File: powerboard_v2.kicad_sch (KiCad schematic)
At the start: 13 parts, among them J4 Conn_01x02_Pin, J5 Conn_01x02_Pin, J6 Conn_01x02_Pin, K1 G6QE-1A DC24, Q1 Q_PMOS, U5 TLP785

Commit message: フットプリントの割り当て
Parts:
- removed Q1: Q_PMOS, symbol Device:Q_PMOS
- added Q2: Q_PMOS_GDS, Package_TO_SOT_THT:TO-220-3_Vertical, symbol Transistor_FET:Q_PMOS_GDS
- C13: footprint (none) -> Capacitor_THT:CP_Radial_D10.0mm_P5.00mm
- D3: footprint (none) -> Diode_SMD:D_SMA
- D4: footprint (none) -> Diode_THT:D_DO-35_SOD27_P7.62mm_Horizontal
- F1: footprint (none) -> Fuse:Fuseholder_Blade_ATO_Littelfuse_Pudenz_2_Pin
- J4: footprint (none) -> Connector_JST:JST_XH_S2B-XH-A-1_1x02_P2.50mm_Horizontal
- J5, J6: footprint (none) -> Connector_AMASS:AMASS_XT60PW-M_1x02_P7.20mm_Horizontal
- R2, R3, R4: footprint (none) -> Resistor_THT:R_Axial_DIN0207_L6.3mm_D2.5mm_P7.62mm_Horizontal
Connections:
- net +24V: now also Q2.2 (D)
- net GND: now also Q2.1 (G)
- net at R4.1: now also Q2.3 (S)
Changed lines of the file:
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@@
+	)
+	(junction
+		(at 78.74 123.19)
+		(diameter 0)
+		(color 0 0 0 0)
 	)
 	(junction
@@
 	(wire
 		(pts
+			(xy 81.28 123.19) (xy 78.74 123.19)
+		)
+		(stroke
+			(width 0)
+			(type default)
+		)
+	)
+	(wire
+		(pts
 			(xy 86.36 35.56) (xy 92.71 35.56)
 		)
@@
 	(wire
 		(pts
+			(xy 78.74 123.19) (xy 78.74 125.73)
+		)
+		(stroke
+			(width 0)
+			(type default)
+		)
+	)
+	(wire
+		(pts
 			(xy 86.36 48.26) (xy 90.17 48.26)
 		)
@@
 	(wire
 		(pts
-			(xy 78.74 120.65) (xy 78.74 125.73)
+			(xy 78.74 120.65) (xy 78.74 123.19)
 		)
 		(stroke
@@
 	(global_label "Photo to Gate"
 		(shape input)
-		(at 78.74 123.19 0)
+		(at 81.28 123.19 0)
 		(fields_autoplaced yes)
 		(effects
@@
 		)
 		(property "Intersheetrefs" "${INTERSHEET_REFS}"
-			(at 95.2111 123.19 0)
+			(at 97.7511 123.19 0)
 			(effects
 				(font
@@
 			)
 		)
-		(property "Footprint" ""
+		(property "Footprint" "Resistor_THT:R_Axial_DIN0207_L6.3mm_D2.5mm_P7.62mm_Horizontal"
 			(at 50.8 113.538 90)
 			(effects
@@
 			)
 		)
-		(property "Footprint" ""
+		(property "Footprint" "Diode_SMD:D_SMA"
 			(at 78.74 90.17 0)
 			(effects
@@
 	)
 	(symbol
+		(lib_id "Transistor_FET:Q_PMOS_GDS")
+		(at 87.63 59.69 0)
+		(unit 1)
+		(exclude_from_sim no)
+		(in_bom yes)
+		(on_board yes)
+		(dnp no)
+		(fields_autoplaced yes)
+		(property "Reference" "Q2"
+			(at 93.98 58.4199 0)
+			(effects
+				(font
+					(size 1.27 1.27)
+				)
+				(justify left)
+			)
+		)
+		(property "Value" "Q_PMOS_GDS"
+			(at 93.98 60.9599 0)
+			(effects
+				(font
+					(size 1.27 1.27)
+				)
+				(justify left)
+			)
+		)
+		(property "Footprint" "Package_TO_SOT_THT:TO-220-3_Vertical"
+			(at 92.71 57.15 0)
+			(effects
+				(font
+					(size 1.27 1.27)
+				)
+				(hide yes)
+			)
+		)
+		(property "Datasheet" "~"
+			(at 87.63 59.69 0)
+			(effects
+				(font
+					(size 1.27 1.27)
+				)
+				(hide yes)
+			)
+		)
+		(property "Description" "P-MOSFET transistor, gate/drain/source"
+			(at 87.63 59.69 0)
+			(effects
+				(font
+					(size 1.27 1.27)
+				)
+				(hide yes)
+			)
+		)
+		(pin "3"
+		)
+		(pin "2"
+		)
+		(pin "1"
+		)
+		(instances
+			(project ""
+				(path "/6e0ca105-c789-4be3-8f3a-c5e169be0bfe"
+					(reference "Q2")
+					(unit 1)
+				)
+			)
+		)
+	)
+	(symbol
 		(lib_id "power:GND")
 		(at 124.46 107.95 0)
@@
 			)
 		)
-		(property "Footprint" ""
+		(property "Footprint" "Capacitor_THT:CP_Radial_D10.0mm_P5.00mm"
 			(at 97.79 47.2948 0)
 			(effects
@@
 			)
 		)
-		(property "Footprint" ""
+		(property "Footprint" "Fuse:Fuseholder_Blade_ATO_Littelfuse_Pudenz_2_Pin"
 			(at 84.582 41.91 90)
 			(effects
@@
 			)
 		)
-		(property "Footprint" ""
+		(property "Footprint" "Connector_JST:JST_XH_S2B-XH-A-1_1x02_P2.50mm_Horizontal"
 			(at 36.83 111.76 0)
 			(effects
@@
 			)
 		)
-		(property "Footprint" ""
+		(property "Footprint" "Resistor_THT:R_Axial_DIN0207_L6.3mm_D2.5mm_P7.62mm_Horizontal"
 			(at 80.518 114.3 90)
 			(effects
@@
 			)
 		)
-		(property "Footprint" ""
+		(property "Footprint" "Diode_THT:D_DO-35_SOD27_P7.62mm_Horizontal"
 			(at 78.74 99.06 0)
 			(effects
@@
 			)
 		)
-		(property "Footprint" ""
+		(property "Footprint" "Resistor_THT:R_Axial_DIN0207_L6.3mm_D2.5mm_P7.62mm_Horizontal"
 			(at 95.25 66.548 90)
 			(effects
@@
 			)
 		)
-		(property "Footprint" ""
+		(property "Footprint" "Connector_AMASS:AMASS_XT60PW-M_1x02_P7.20mm_Horizontal"
 			(at 132.08 97.79 0)
 			(effects
@@
 			)
 		)
-		(property "Footprint" ""
+		(property "Footprint" "Connector_AMASS:AMASS_XT60PW-M_1x02_P7.20mm_Horizontal"
 			(at 95.25 30.48 0)
 			(effects
@@
 					(unit 1)
 				)
-			)
-		)
-	)
-	(symbol
-		(lib_id "Device:Q_PMOS")
-		(at 87.63 59.69 0)
-		(mirror x)
-		(unit 1)
-		(exclude_from_sim no)
-		(in_bom yes)
-		(on_board yes)
-		(dnp no)
-		(property "Reference" "Q1"
-			(at 91.948 56.134 0)
-			(effects
-				(font
-					(size 1.27 1.27)
-				)
-			)
-		)
-		(property "Value" "Q_PMOS"
-			(at 84.328 56.388 0)
-			(effects
-				(font
-					(size 1.27 1.27)
-				)
-			)
-		)
-		(property "Footprint" ""
-			(at 92.71 62.23 0)
-			(effects
-				(font
-					(size 1.27 1.27)
-				)
-				(hide yes)
-			)
-		)
-		(property "Datasheet" "~"
-			(at 87.63 59.69 0)
-			(effects
-				(font
-					(size 1.27 1.27)
-				)
-				(hide yes)
-			)
-		)
-		(property "Description" "P-MOSFET transistor"
-			(at 87.63 59.69 0)
-			(effects
-				(font
-					(size 1.27 1.27)
-				)
-				(hide yes)
-			)
-		)
-		(pin "S"
-		)
-		(pin "D"
-		)
-		(pin "G"
-		)
-		(instances
-			(project ""
-				(path "/6e0ca105-c789-4be3-8f3a-c5e169be0bfe"
-					(reference "Q1")
-					(unit 1)
-				)

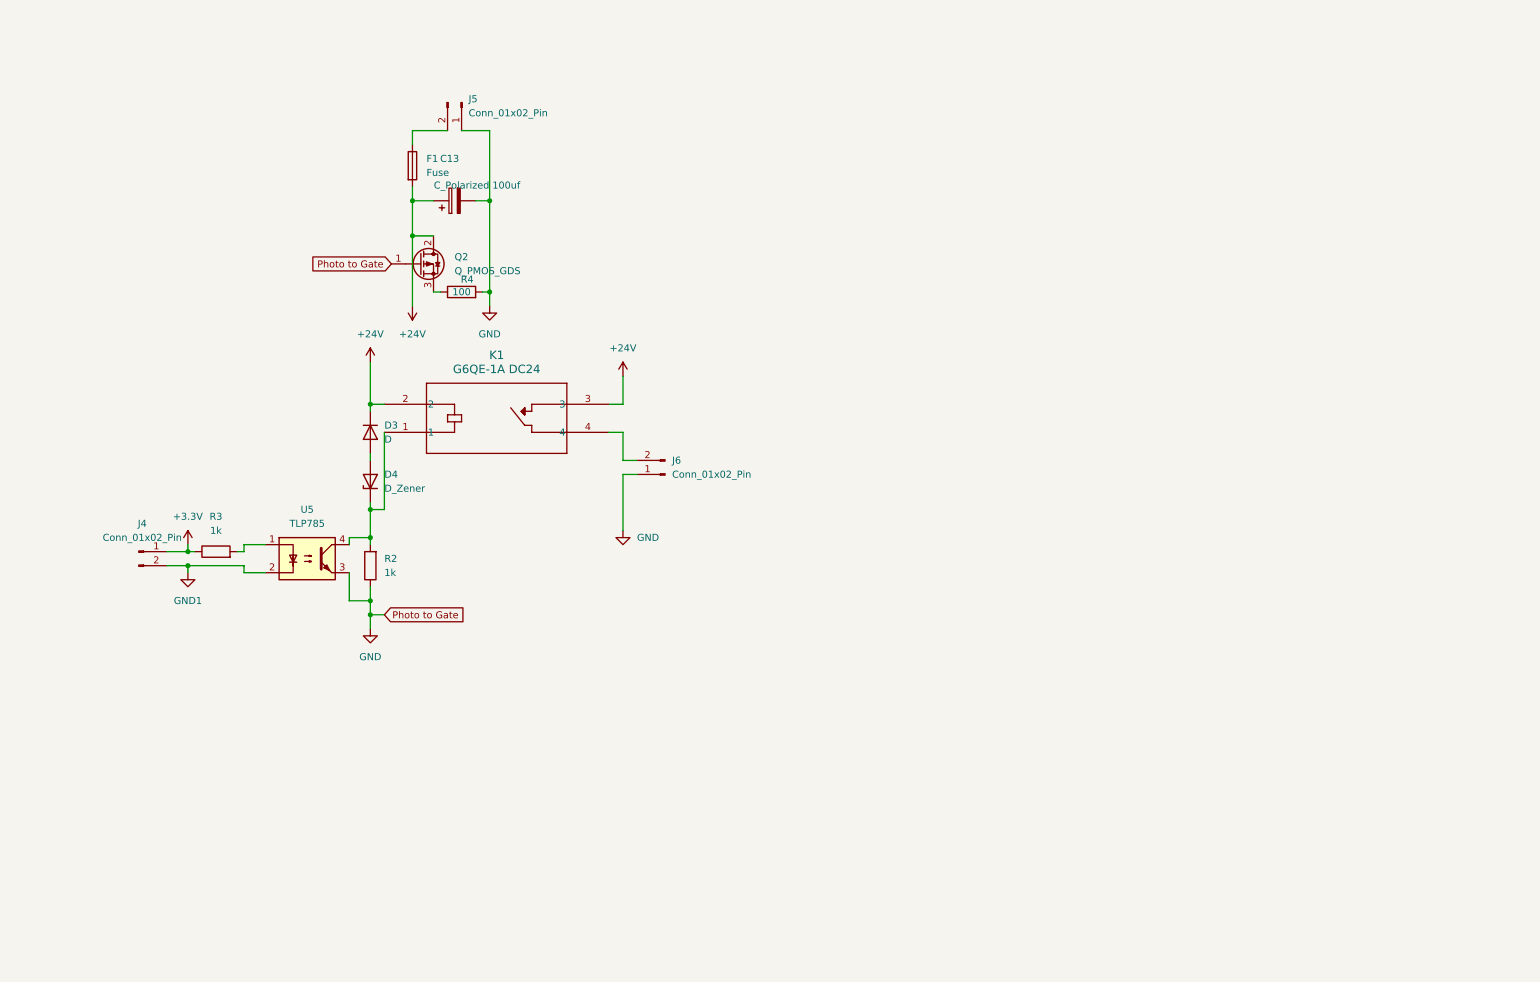
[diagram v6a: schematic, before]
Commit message: 回路構成の変更、フットプリントの割り当て、部品配置
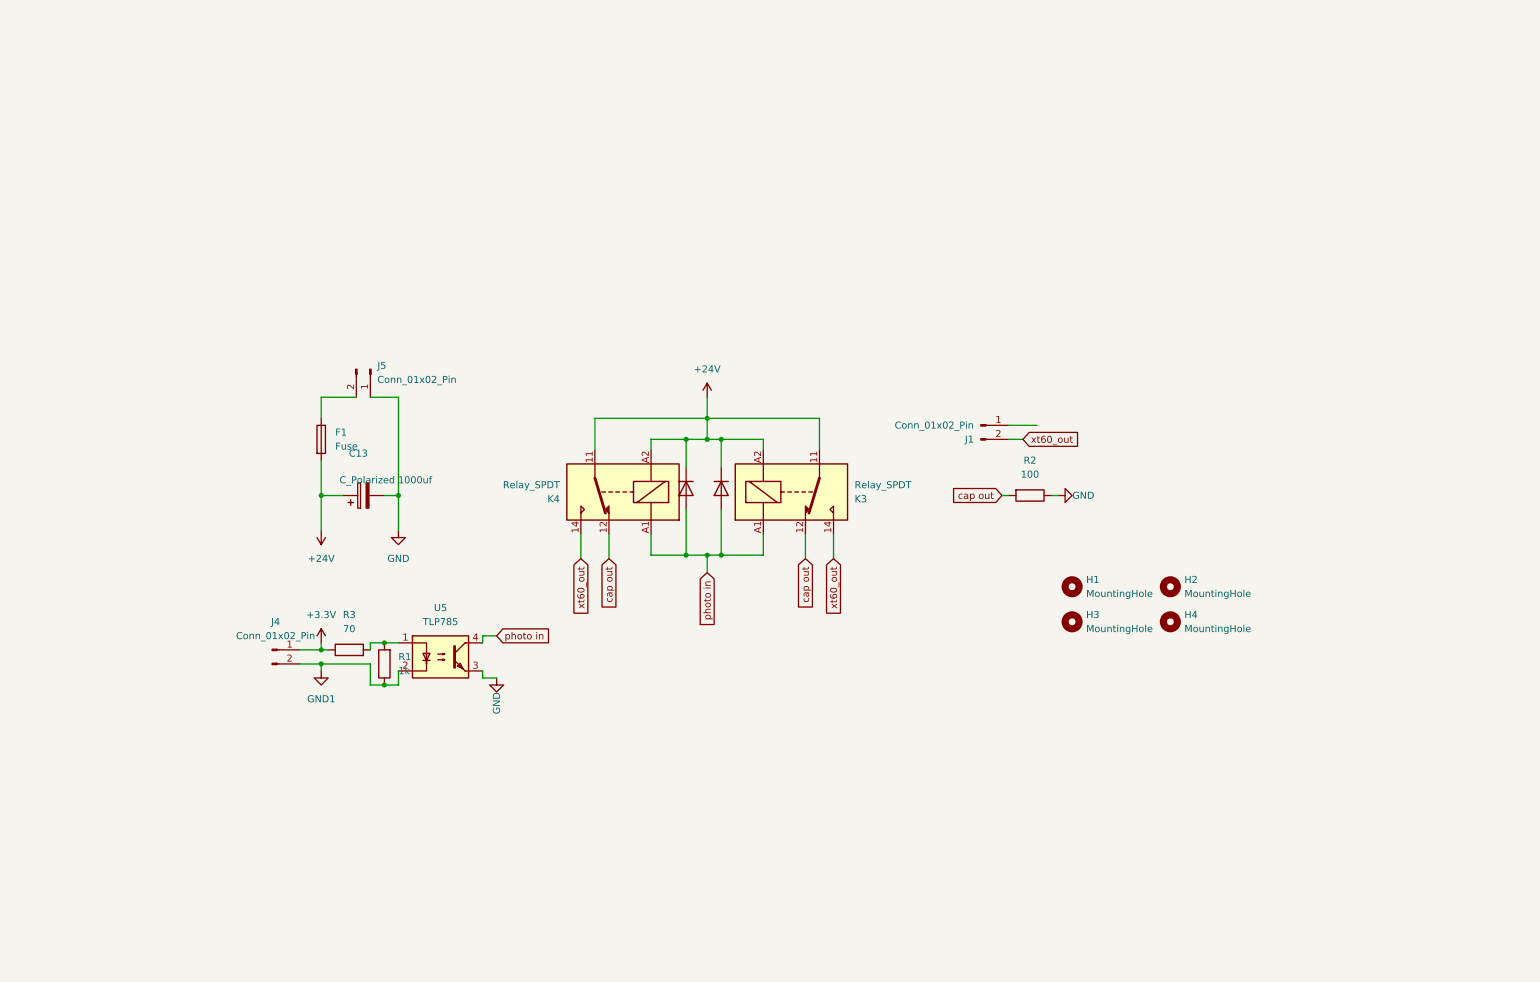
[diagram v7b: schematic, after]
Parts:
- removed D4: D_Zener, Diode_THT:D_DO-35_SOD27_P7.62mm_Horizontal, symbol Device:D_Zener
- removed J6: Conn_01x02_Pin, Connector_AMASS:AMASS_XT60PW-M_1x02_P7.20mm_Horizontal, symbol Connector:Conn_01x02_Pin
- removed K1: G6QE-1A DC24, footprints:RELAY_G6QE-1A_OMR, symbol 2026-04-11_13-59-38:G6QE-1A_DC24
- removed Q2: Q_PMOS_GDS, Package_TO_SOT_THT:TO-220-3_Vertical, symbol Transistor_FET:Q_PMOS_GDS
- removed R4: 100, Resistor_THT:R_Axial_DIN0207_L6.3mm_D2.5mm_P7.62mm_Horizontal, symbol Device:R
- added D1: D, Diode_SMD:D_SMA, symbol Device:D
- added H1, H2, H3, H4: MountingHole, MountingHole:MountingHole_3.2mm_M3, symbol Mechanical:MountingHole
- added J1: Conn_01x02_Pin, Connector_AMASS:AMASS_XT60PW-M_1x02_P7.20mm_Horizontal, symbol Connector:Conn_01x02_Pin
- added K3, K4: Relay_SPDT, Relay_THT:Relay_SPDT_RAYEX-L90S, symbol Relay:Relay_SPDT
- added R1: 1k, Resistor_THT:R_Axial_DIN0207_L6.3mm_D2.5mm_P7.62mm_Horizontal, symbol Device:R
- C13: value C_Polarized 100uf -> C_Polarized 1000uf; footprint Capacitor_THT:CP_Radial_D10.0mm_P5.00mm -> Capacitor_THT:CP_Radial_D12.5mm_P5.00mm
- R2: value 1k -> 100; footprint Resistor_THT:R_Axial_DIN0207_L6.3mm_D2.5mm_P7.62mm_Horizontal -> Resistor_THT:R_Axial_DIN0516_L15.5mm_D5.0mm_P7.62mm_Vertical
- R3: value 1k -> 70
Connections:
- net +24V: now also D1.1 (K), K3.11, K3.A2, K4.11, K4.A2
- net GND1: now also R1.1
- net at R3.2, U5.1: now also R1.2
- net photo in: now reaches D3.2 (A)
- net photo in: now also U5.4, D1.2 (A), K3.A1, K4.A1
- net cap out: now reaches R2.2
- net cap out: now also K3.12, K4.12; no longer U5.4
- new net xt60_out: J1.2 (Pin_2), K3.14, K4.14
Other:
- moved on the sheet: C13, F1, J4, J5, R3, U5

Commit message: 配線前最終版
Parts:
- removed F1: Fuse, Fuse:Fuseholder_Blade_ATO_Littelfuse_Pudenz_2_Pin, symbol Device:Fuse
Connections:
- net +24V: now also D1.2 (A), D3.2 (A), J5.2 (Pin_2), K3.14, K3.A1, K4.14, K4.A1; no longer C13.1, D1.1 (K), D3.1 (K), K3.11, K3.A2, K4.11, K4.A2
- net GND: now also J1.1 (Pin_1)
- net photo in: now also D1.1 (K), D3.1 (K), K3.A2, K4.A2; no longer D1.2 (A), D3.2 (A), K3.A1, K4.A1
- net xt60_out: now also C13.1, K3.11, K4.11; no longer K3.14, K4.14
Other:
- moved on the sheet: C13, H1, H2, H3, H4, J1, J4, J5, K3, K4, R1, R2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
